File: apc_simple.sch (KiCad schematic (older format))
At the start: 16 parts, among them J1 Output, U1 NE556

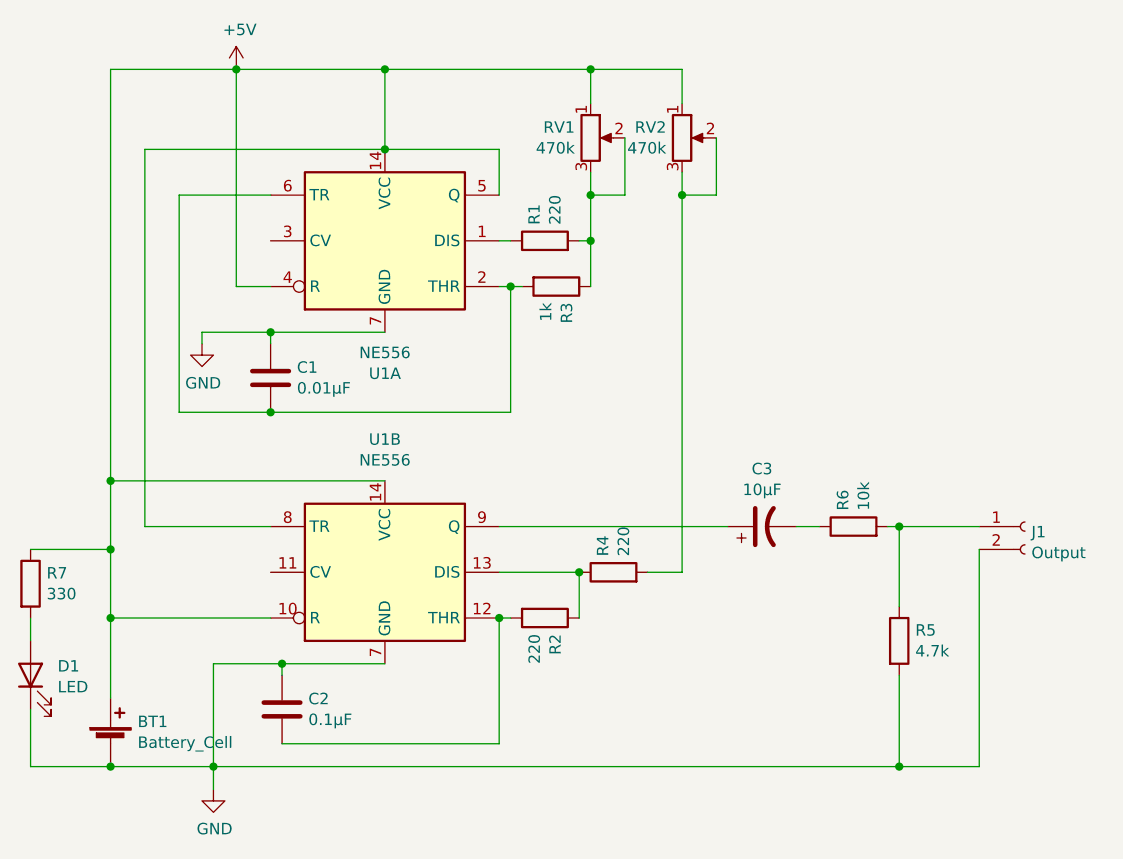
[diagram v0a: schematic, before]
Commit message: Fixed error in schematic; re-designed breadboard wiring
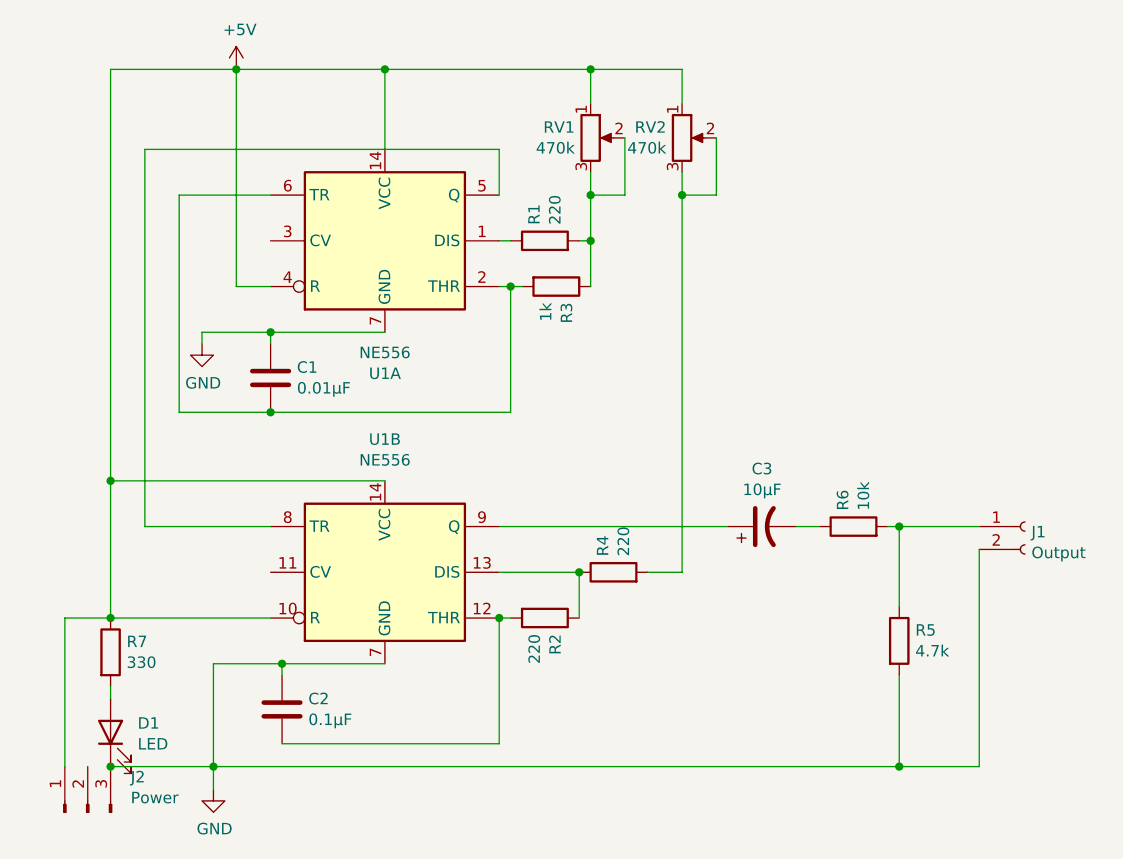
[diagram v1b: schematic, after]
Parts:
- removed BT1: Battery_Cell, Connector_PinHeader_2.54mm:PinHeader_1x02_P2.54mm_Vertical, symbol Device:Battery_Cell
- added J2: Power, Connector_PinHeader_2.54mm:PinHeader_1x03_P2.54mm_Vertical, symbol Connector:Conn_01x03_Male
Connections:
- net +5V: now also J2.1 (Pin_1); no longer U1.5 (Q), U1.8 (TR)
- net GND: now also J2.3 (Pin_3)
- new net: U1.5 (Q), U1.8 (TR)
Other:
- moved on the sheet: D1, R7
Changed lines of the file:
@@
 encoding utf-8
 Sheet 1 1
-Title "APC Schematic"
+Title "APC Simple with LED"
 Date "2022-07-03"
 Rev "v1"
@@
 	5850 3100 5850 2900
 Wire Wire Line
-	5850 2900 5350 2900
-Wire Wire Line
 	4300 2900 4300 4550
 Wire Wire Line
 	4300 4550 4850 4550
-Connection ~ 5350 2900
-Wire Wire Line
-	5350 2900 4300 2900
 $Comp
 L Device:R R1
@@
 	4850 4950 4150 4950
 Wire Wire Line
-	4150 4950 4150 4650
-Wire Wire Line
 	4150 2550 4700 2550
 Wire Wire Line
@@
 	7600 5200 7600 5600
 Connection ~ 7600 5600
-Connection ~ 4150 4950
 Wire Wire Line
 	7600 4550 7950 4550
@@
 Wire Wire Line
 	7950 4650 7950 5600
-$Comp
-L Device:Battery_Cell BT1
-U 1 1 62D5D59D
-P 4150 5500
-F 0 "BT1" H 4268 5596 50  0000 L CNN
-F 1 "Battery_Cell" H 4268 5505 50  0000 L CNN
-F 2 "Connector_PinHeader_2.54mm:PinHeader_1x02_P2.54mm_Vertical" V 4150 5560 50  0001 C CNN
-F 3 "~" V 4150 5560 50  0001 C CNN
-	1    4150 5500
-	1    0    0    -1
-$EndComp
-Wire Wire Line
-	4150 5300 4150 4950
 Wire Wire Line
 	6250 2550 6650 2550
@@
 L Device:LED D1
 U 1 1 62D79BD1
-P 3800 5200
-F 0 "D1" V 3839 5082 50  0000 R CNN
-F 1 "LED" V 3748 5082 50  0000 R CNN
-F 2 "LED_THT:LED_D5.0mm" H 3800 5200 50  0001 C CNN
-F 3 "~" H 3800 5200 50  0001 C CNN
-	1    3800 5200
+P 4150 5450
+F 0 "D1" V 4189 5332 50  0000 R CNN
+F 1 "LED" V 4098 5332 50  0000 R CNN
+F 2 "LED_THT:LED_D5.0mm" H 4150 5450 50  0001 C CNN
+F 3 "~" H 4150 5450 50  0001 C CNN
+	1    4150 5450
 	0    -1   -1   0
 $EndComp
@@
 L Device:R R7
 U 1 1 62D7C0B3
-P 3800 4800
-F 0 "R7" H 3870 4846 50  0000 L CNN
-F 1 "330" H 3870 4755 50  0000 L CNN
-F 2 "Resistor_THT:R_Axial_DIN0411_L9.9mm_D3.6mm_P12.70mm_Horizontal" V 3730 4800 50  0001 C CNN
-F 3 "~" H 3800 4800 50  0001 C CNN
-	1    3800 4800
-	1    0    0    -1
-$EndComp
-Wire Wire Line
-	3800 5350 3800 5600
-Wire Wire Line
-	3800 5600 4150 5600
+P 4150 5100
+F 0 "R7" H 4220 5146 50  0000 L CNN
+F 1 "330" H 4220 5055 50  0000 L CNN
+F 2 "Resistor_THT:R_Axial_DIN0411_L9.9mm_D3.6mm_P12.70mm_Horizontal" V 4080 5100 50  0001 C CNN
+F 3 "~" H 4150 5100 50  0001 C CNN
+	1    4150 5100
+	1    0    0    -1
+$EndComp
+Wire Wire Line
+	4150 5600 4600 5600
+Connection ~ 4150 4950
+Wire Wire Line
+	4150 4350 4150 4950
+Wire Wire Line
+	4150 5300 4150 5250
+$Comp
+L Connector:Conn_01x03_Male J2
+U 1 1 62EADCC3
+P 4050 5800
+F 0 "J2" V 4204 5612 50  0000 R CNN
+F 1 "Power" V 4113 5612 50  0000 R CNN
+F 2 "Connector_PinHeader_2.54mm:PinHeader_1x03_P2.54mm_Vertical" H 4050 5800 50  0001 C CNN
+F 3 "~" H 4050 5800 50  0001 C CNN
+	1    4050 5800
+	0    -1   -1   0
+$EndComp
 Connection ~ 4150 5600
 Wire Wire Line
-	4150 5600 4600 5600
-Wire Wire Line
-	3800 4950 3800 5050
-Wire Wire Line
-	4150 4650 3800 4650
-Connection ~ 4150 4650
-Wire Wire Line
-	4150 4650 4150 4350
+	4150 4950 3950 4950
+Wire Wire Line
+	3950 4950 3950 5600
+Wire Wire Line
+	4300 2900 5850 2900
 $EndSCHEMATC

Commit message: Rewire 1k resistor directly between THR and DIS
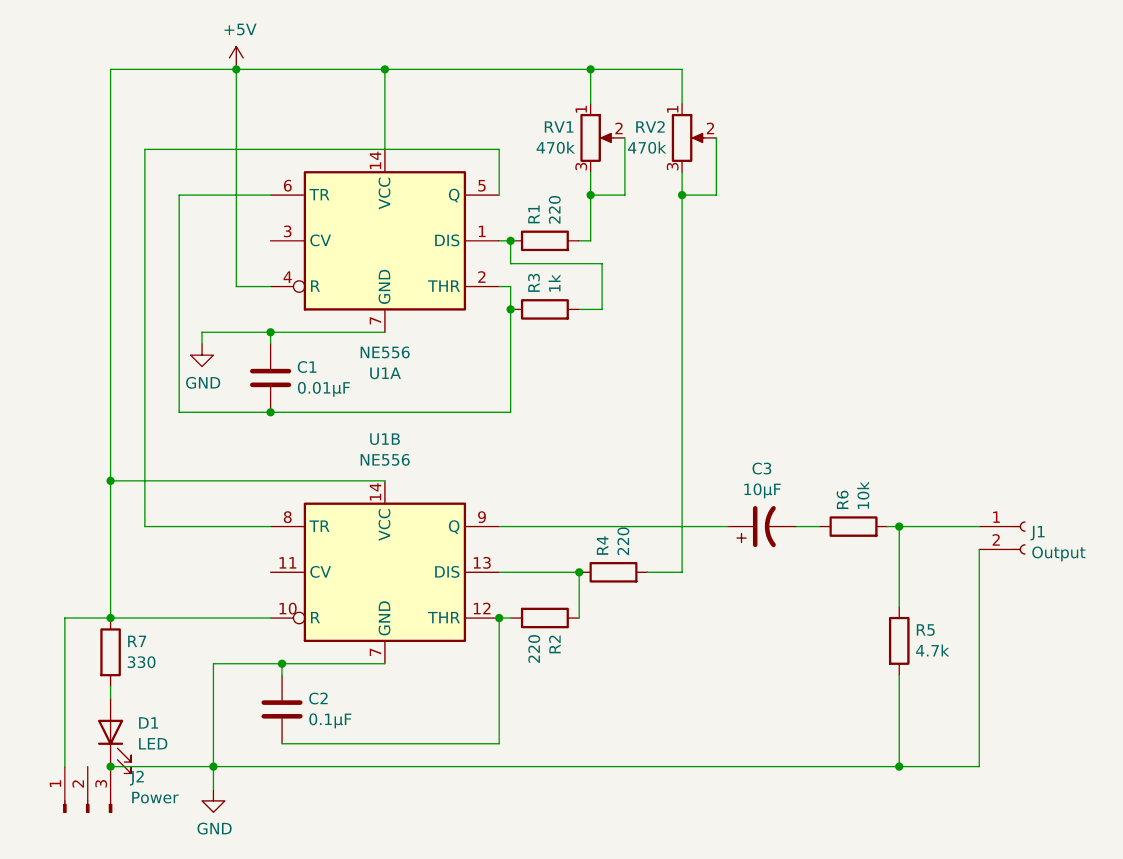
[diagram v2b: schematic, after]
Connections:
- net at R1.1, U1.1 (DIS): now also R3.2
- net at C1.2, U1.2 (THR), U1.6 (TR): now also R3.1; no longer R3.2
- net at R1.2, RV1.2, RV1.3: no longer R3.1
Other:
- moved on the sheet: R3
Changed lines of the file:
@@
-$EndComp
-$Comp
-L Timer:NE556 U1
-U 1 1 62810120
-P 5350 3300
-F 0 "U1" H 5350 2719 50  0000 C CNN
-F 1 "NE556" H 5350 2810 50  0000 C CNN
-F 2 "Package_DIP:DIP-14_W7.62mm_Socket" H 5350 3300 50  0001 C CNN
-F 3 "http://www.ti.com/lit/ds/symlink/ne556.pdf" H 5350 3300 50  0001 C CNN
-	1    5350 3300
-	1    0    0    -1
 $EndComp
 $Comp
@@
 L Device:R R3
 U 1 1 62818D6F
-P 6100 3500
-F 0 "R3" H 6170 3546 50  0000 L CNN
-F 1 "1k" H 6170 3455 50  0000 L CNN
-F 2 "Resistor_THT:R_Axial_DIN0411_L9.9mm_D3.6mm_P12.70mm_Horizontal" V 6030 3500 50  0001 C CNN
-F 3 "~" H 6100 3500 50  0001 C CNN
-	1    6100 3500
-	0    1    1    0
+P 6050 3600
+F 0 "R3" H 6120 3646 50  0000 L CNN
+F 1 "1k" H 6120 3555 50  0000 L CNN
+F 2 "Resistor_THT:R_Axial_DIN0411_L9.9mm_D3.6mm_P12.70mm_Horizontal" V 5980 3600 50  0001 C CNN
+F 3 "~" H 6050 3600 50  0001 C CNN
+	1    6050 3600
+	0    -1   -1   0
 $EndComp
 Wire Wire Line
@@
 	4850 4050 5900 4050
 Wire Wire Line
-	5900 4050 5900 3500
+	5900 4050 5900 3600
 Connection ~ 4850 4050
-Connection ~ 5900 3500
-Wire Wire Line
-	5900 3500 5950 3500
 Wire Wire Line
 	4850 3500 4700 3500
@@
 	6250 3000 6250 3100
 Wire Wire Line
-	5850 3300 5900 3300
-Wire Wire Line
-	6200 3300 6250 3300
-Connection ~ 6250 3300
-Wire Wire Line
-	6250 3300 6250 3500
+	6250 3100 6400 3100
 $Comp
 L Device:R_POT RV2
@@
 	6400 2850 6400 3100
 Wire Wire Line
-	6400 3100 6250 3100
-Connection ~ 6250 3100
-Wire Wire Line
-	6250 3100 6250 3300
-Wire Wire Line
 	6800 2850 6800 3100
 Wire Wire Line
@@
 Wire Wire Line
 	4300 2900 5850 2900
+Wire Wire Line
+	6300 3600 6200 3600
+Connection ~ 5900 3600
+Wire Wire Line
+	5900 3600 5900 3500
+$Comp
+L Timer:NE556 U1
+U 1 1 62810120
+P 5350 3300
+F 0 "U1" H 5350 2719 50  0000 C CNN
+F 1 "NE556" H 5350 2810 50  0000 C CNN
+F 2 "Package_DIP:DIP-14_W7.62mm_Socket" H 5350 3300 50  0001 C CNN
+F 3 "http://www.ti.com/lit/ds/symlink/ne556.pdf" H 5350 3300 50  0001 C CNN
+	1    5350 3300
+	1    0    0    -1
+$EndComp
+Wire Wire Line
+	6300 3400 6300 3600
+Wire Wire Line
+	5900 3400 6300 3400
+Wire Wire Line
+	5900 3400 5900 3300
+Wire Wire Line
+	5850 3300 5900 3300
+Connection ~ 5900 3300
+Wire Wire Line
+	6250 3100 6250 3300
+Wire Wire Line
+	6250 3300 6200 3300
+Connection ~ 6250 3100
 $EndSCHEMATC

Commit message: Make it fit 19x19 strip mask
Switch around some connectors and footprints.
Mark strip mask lane cutting marks on backside "silk screen".
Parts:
- J2: symbol Connector:Conn_01x03_Male -> Connector:Conn_01x02_Male
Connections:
- net GND: now also J2.2 (Pin_2); no longer J2.3 (Pin_3)
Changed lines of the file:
@@
 Wire Wire Line
 	4150 5300 4150 5250
-$Comp
-L Connector:Conn_01x03_Male J2
-U 1 1 62EADCC3
-P 4050 5800
-F 0 "J2" V 4204 5612 50  0000 R CNN
-F 1 "Power" V 4113 5612 50  0000 R CNN
-F 2 "Connector_PinHeader_2.54mm:PinHeader_1x03_P2.54mm_Vertical" H 4050 5800 50  0001 C CNN
-F 3 "~" H 4050 5800 50  0001 C CNN
-	1    4050 5800
-	0    -1   -1   0
-$EndComp
-Connection ~ 4150 5600
 Wire Wire Line
-	4150 4950 3950 4950
-Wire Wire Line
-	3950 4950 3950 5600
+	4150 4950 4050 4950
 Wire Wire Line
 	4300 2900 5850 2900
@@
 	6250 3300 6200 3300
 Connection ~ 6250 3100
+Connection ~ 4150 5600
+Wire Wire Line
+	4050 4950 4050 5600
+$Comp
+L Connector:Conn_01x02_Male J2
+U 1 1 62EADCC3
+P 4050 5800
+F 0 "J2" V 4204 5612 50  0000 R CNN
+F 1 "Power" V 4113 5612 50  0000 R CNN
+F 2 "Connector_PinHeader_2.54mm:PinHeader_1x03_P2.54mm_Vertical" H 4050 5800 50  0001 C CNN
+F 3 "~" H 4050 5800 50  0001 C CNN
+	1    4050 5800
+	0    -1   -1   0
+$EndComp
 $EndSCHEMATC
